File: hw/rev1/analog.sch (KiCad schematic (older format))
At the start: 69 parts, among them J1 80VAC, J2 CAP, J3 MOTOR, J5 TACHO, Q1 6N60C, Q2 2N5551, Q4 2N5551, U1 LM324, U2 LM311

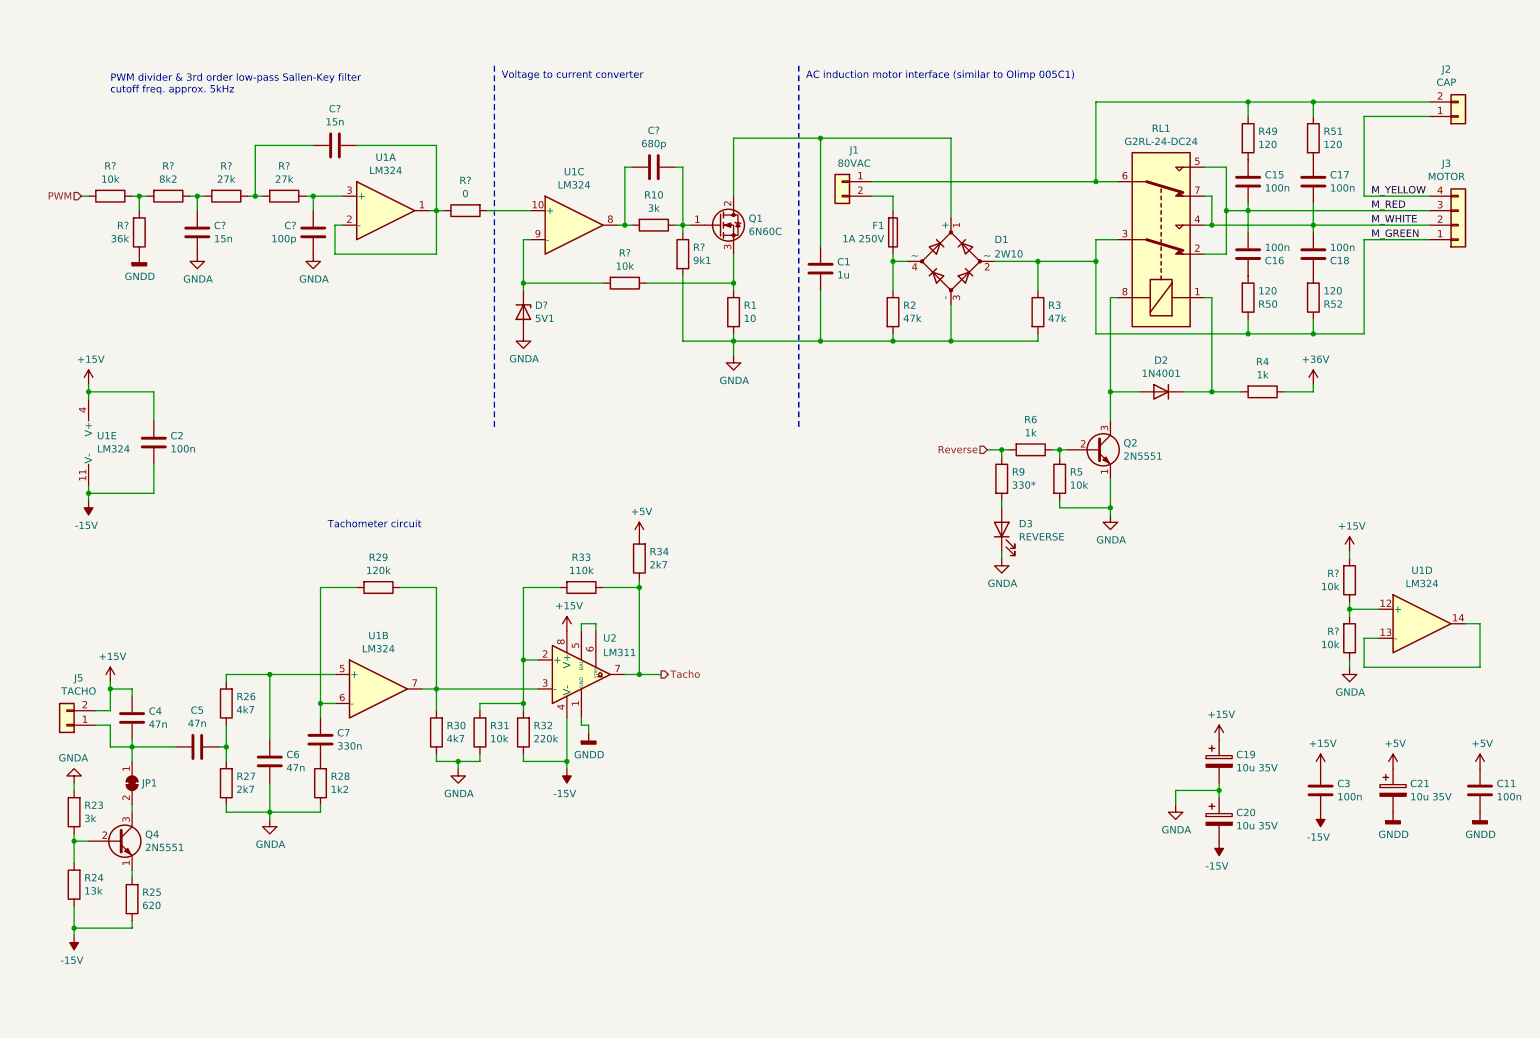
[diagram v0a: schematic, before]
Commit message: В схему добавлен забытый ZCD.
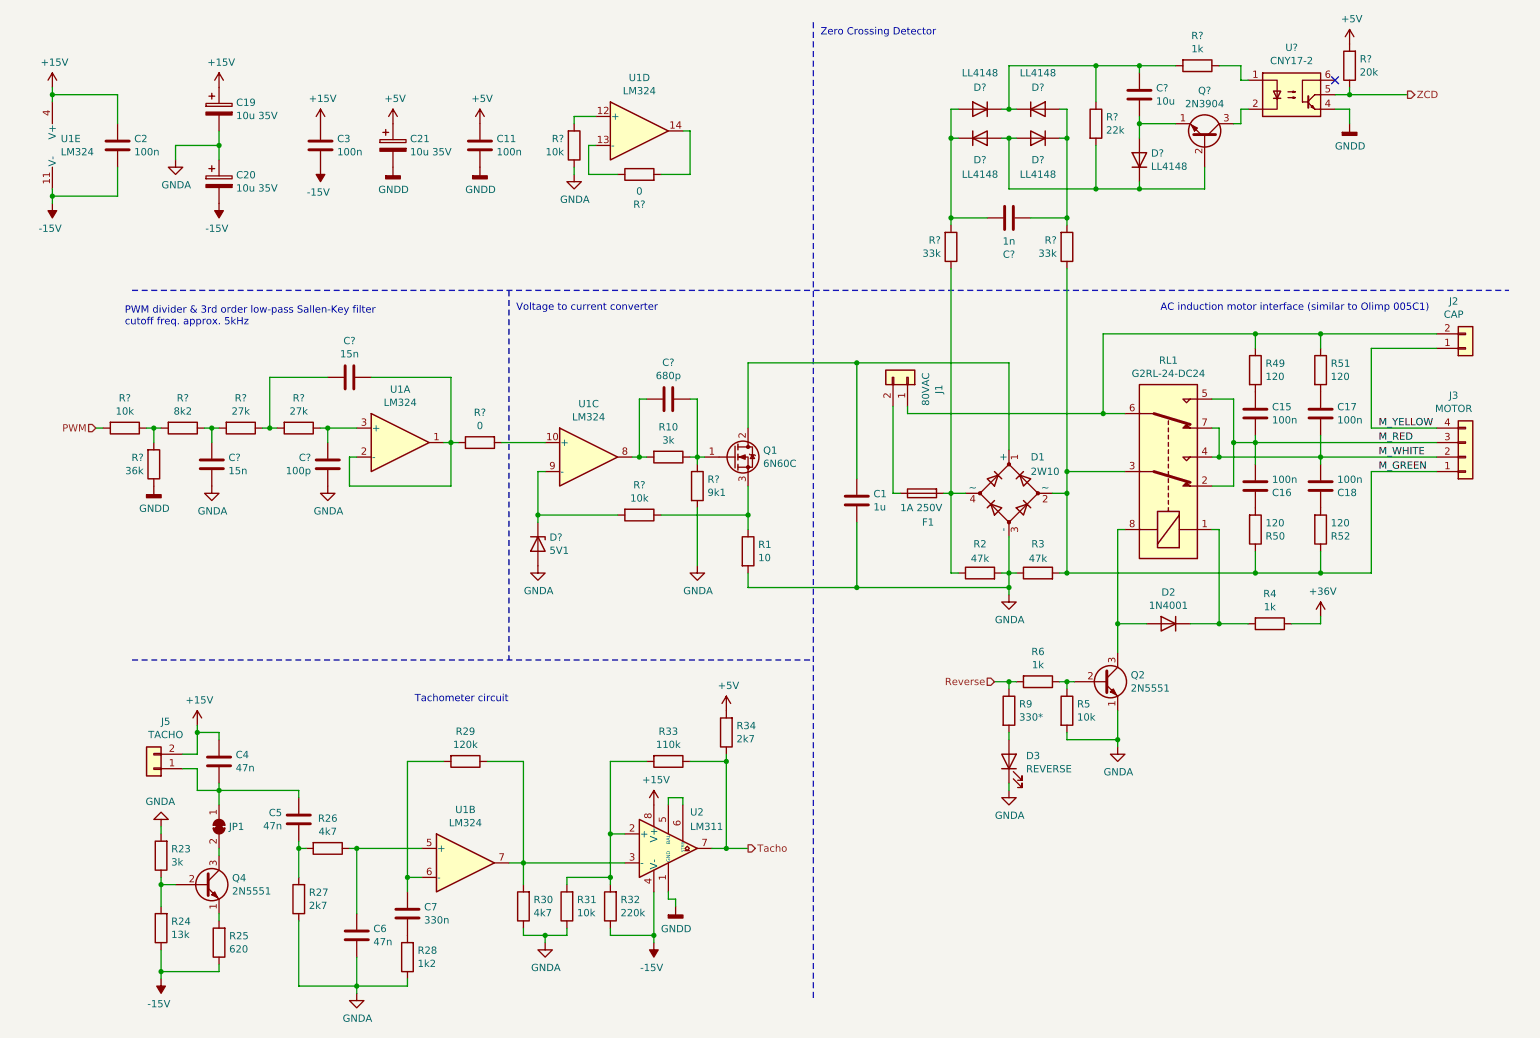
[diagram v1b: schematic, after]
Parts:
- removed R?: 10k, Resistor_SMD:R_0805_2012Metric, symbol Device:R
- added C?: 1n, Capacitor_SMD:C_0805_2012Metric, symbol Device:C
- added C?: 10u, Capacitor_SMD:C_0805_2012Metric, symbol Device:C
- added D? (x5): LL4148, Diode_SMD:D_MiniMELF, symbol Diode:LL4148
- added Q?: 2N3904, Package_TO_SOT_THT:TO-92_Inline, symbol Transistor_BJT:2N3904
- added R?: 0, Resistor_SMD:R_0805_2012Metric, symbol Device:R
- added R? (x2): 33k, Resistor_SMD:R_0805_2012Metric, symbol Device:R
- added R?: 22k, Resistor_THT:R_Axial_DIN0207_L6.3mm_D2.5mm_P10.16mm_Horizontal, symbol Device:R
- added R?: 1k, Resistor_THT:R_Axial_DIN0207_L6.3mm_D2.5mm_P10.16mm_Horizontal, symbol Device:R
- added R?: 20k, Resistor_SMD:R_0805_2012Metric, symbol Device:R
- added U?: CNY17-2, symbol Isolator:CNY17-2
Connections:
- net +15V: no longer R?.2
- net +5V: now also R?.2
- net GNDA: now also R3.1, R?.1; no longer R3.2
- net GNDD: now also U?.4
- net M_GREEN: now also R3.2, R?.1; no longer R3.1
- net at J1.2 (Pin_2): now also F1.1; no longer F1.2
- net at D1.4 (~~), R2.1: now also F1.2, R?.1; no longer F1.1
- net at C4.2, J5.1 (Pin_1), JP1.1 (A): now also C5.1; no longer C5.2
- net at C6.1, U1.5 (+): now also R26.1; no longer R26.2
- net at U1.12 (+): now also R?.2; no longer R?.1
- net at U1.13 (-): now also R?.1; no longer U1.14
- new net: R?.2, U1.14
- new net: C5.2, R26.2, R27.2
- new net: C?.2, D?.1 (K), D?.2 (A), R?.2
- new net: D?.1 (K), D?.2 (A), D?.2 (A), Q?.2 (B), R?.2
- new net: C?.1, D?.1 (K), D?.1 (K), R?.1, R?.2
- new net: C?.1, D?.1 (K), D?.2 (A), R?.2
- new net: C?.2, D?.2 (A), Q?.1 (E)
- new net: Q?.3 (C), U?.2
- new net: R?.1, U?.1
- new net ZCD: R?.1, U?.5
- no-connect marks 0 -> 1
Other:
- note added: "Zero Crossing Detector"
- moved on the sheet: C1, C11, C15, C16, C17, C18, C19, C2, C20, C21, C3, C4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

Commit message: Добавлена печатная плата rev1 (вероятно чистовая).
+ Обозначена и разведена схема ZCD;
+ Исключена схема аналогового перемножителя;
  * модуляция модулем синуса полностью цифровая;
+ LM324 использована полностью:
  * собран 2й PWM фильтр, подключенный к OC2A в отладочных целях;
+ Добавлен доп. светодиод, предназначенный для контроля за ZCD;
+ Исправлен разъем логических сигналов управления;
+ Всякие незначимые украшательства.
+ Немного документирована плата rev0.
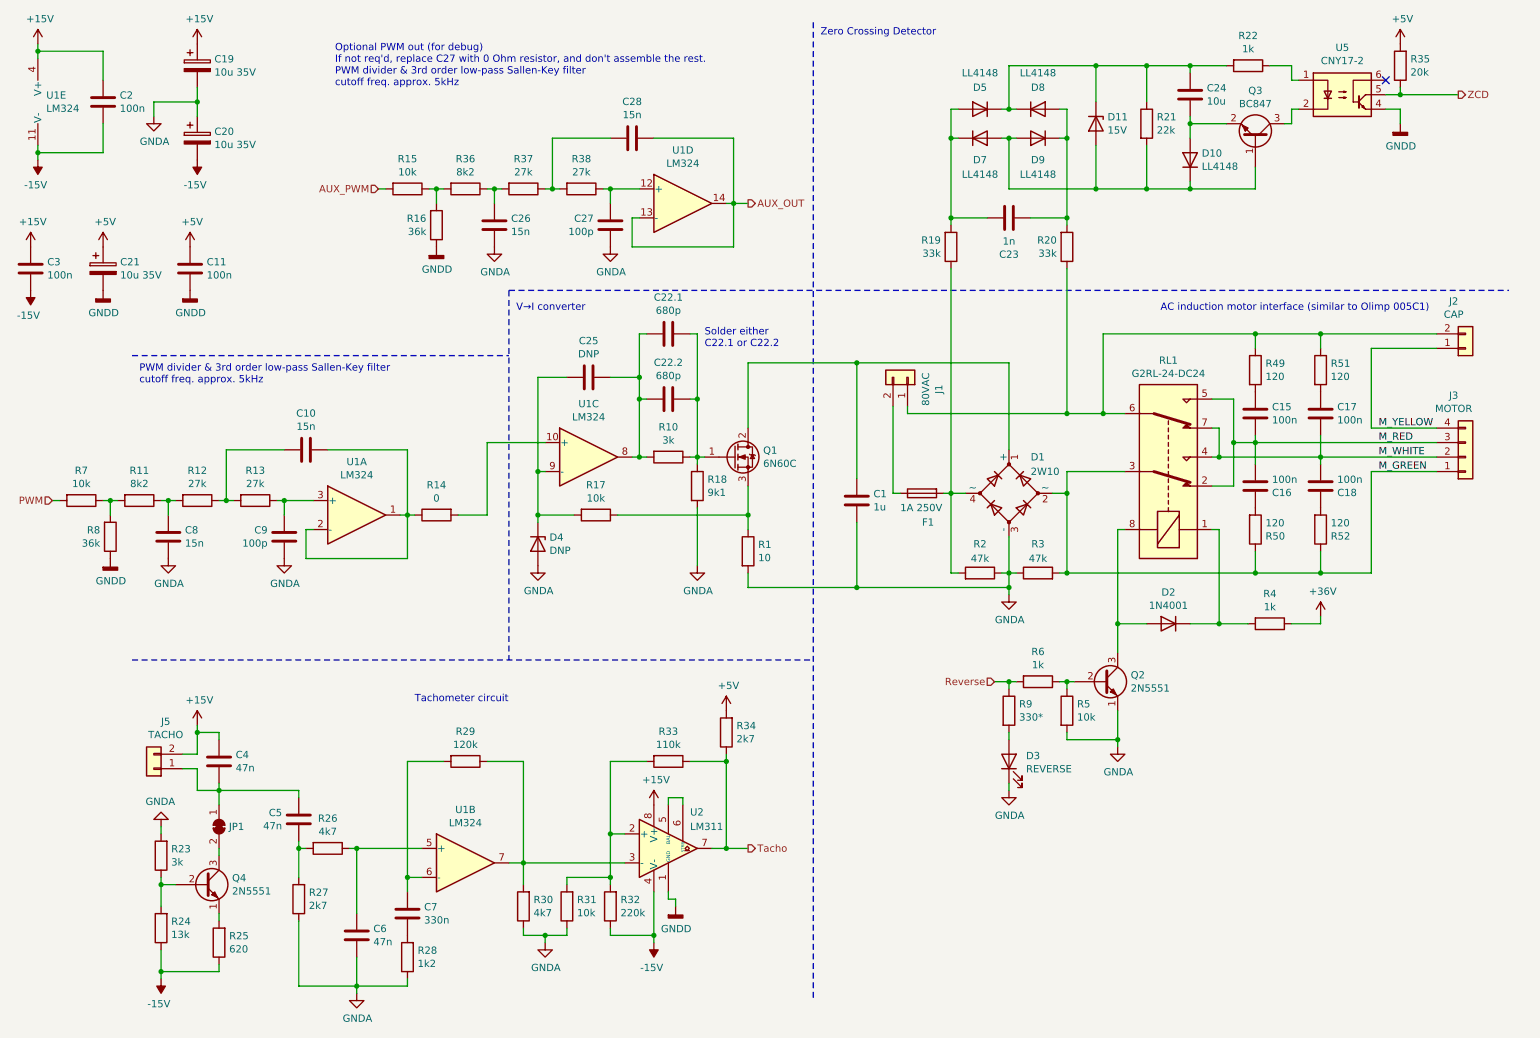
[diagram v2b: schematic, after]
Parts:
- removed Q?: 2N3904, Package_TO_SOT_THT:TO-92_Inline, symbol Transistor_BJT:2N3904
- removed R?: 0, Resistor_SMD:R_0805_2012Metric, symbol Device:R
- removed R?: 1k, Resistor_THT:R_Axial_DIN0207_L6.3mm_D2.5mm_P10.16mm_Horizontal, symbol Device:R
- removed R?: 10k, Resistor_SMD:R_0805_2012Metric, symbol Device:R
- added C22.1: 680p, Capacitor_THT:C_Rect_L7.0mm_W4.5mm_P5.00mm, symbol Device:C
- added C25: DNP, Capacitor_SMD:C_0805_2012Metric, symbol Device:C
- added C26, C28: 15n, Capacitor_SMD:C_0805_2012Metric, symbol Device:C
- added C27: 100p, Capacitor_SMD:C_0805_2012Metric, symbol Device:C
- added D11: 15V, Diode_SMD:D_SOD-123, symbol Device:D_Zener
- added Q3: BC847, Package_TO_SOT_SMD:SOT-23, symbol Transistor_BJT:BC847
- added R15: 10k, Resistor_SMD:R_0805_2012Metric, symbol Device:R
- added R16: 36k, Resistor_SMD:R_0805_2012Metric, symbol Device:R
- added R22: 1k, Resistor_SMD:R_1206_3216Metric, symbol Device:R
- added R36: 8k2, Resistor_SMD:R_0805_2012Metric, symbol Device:R
- added R37, R38: 27k, Resistor_SMD:R_0805_2012Metric, symbol Device:R
- C23, C24: renamed from C?; footprint Capacitor_SMD:C_0805_2012Metric -> Capacitor_SMD:C_1206_3216Metric
- D4: renamed from D?; value 5V1 -> DNP; footprint (none) -> Diode_SMD:D_SOD-123
- Q1: footprint to220:TO-220F-3_Horizontal_TabDown -> to220:TO-220F-3_Horizontal_TabDown_no_silk
- R19, R20: renamed from R?; footprint Resistor_SMD:R_0805_2012Metric -> Resistor_SMD:R_1206_3216Metric
- R21: renamed from R?; footprint Resistor_THT:R_Axial_DIN0207_L6.3mm_D2.5mm_P10.16mm_Horizontal -> Resistor_SMD:R_1206_3216Metric
- U5: renamed from U?; footprint (none) -> Package_DIP:DIP-6_W7.62mm_LongPads
- gave numbers to parts that had none: 18
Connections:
- net GNDA: now also R2.1, C26.2, C27.2; no longer R2.2
- net GNDD: now also R16.1
- net M_GREEN: no longer R20.1
- net at J1.1 (Pin_1), J2.2 (Pin_2), R49.1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: now also R20.1
- net at D1.4 (~~), F1.2, R19.1: now also R2.2; no longer R2.1
- net at C22.2.1, Q1.1 (G), R10.1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: now also C22.1.1
- net at C22.2.2, R10.2, U1.8: now also C22.1.2, C25.1
- net AUX_OUT: now reaches U1.13 (-)
- net AUX_OUT: now also U1.14, C28.1
- net at D4.1 (K), R17.2, U1.9 (-): now also C25.2
- net at D10.1 (K), D7.2 (A), D9.2 (A)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: now also D11.2 (A), Q3.1 (B)
- net at C24.1, D5.1 (K), D8.1 (K)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: now also D11.1 (K), R22.2
- net at C24.2, D10.2 (A): now also Q3.2 (E)
- net at U5.2: now also Q3.3 (C)
- net at U5.1: now also R22.1
- net at U1.12 (+): now also C27.1, R38.1
- new net: C28.2, R37.1, R38.2
- new net: C26.1, R36.1, R37.2
- new net: R15.1, R16.2, R36.2
- new net AUX_PWM: R15.2
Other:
- note added: "Optional PWM out (for debug)\nIf not req'd, replace C27 with 0 Ohm resistor, and don't assemble the rest.\nPWM divider & 3rd order low-pass Sallen-Key filter\ncutoff freq. approx. 5kHz"
- note added: "Solder either\nC22.1 or C22.2"
- note added: "V→I converter"
- note removed: "Voltage to current converter"
- moved on the sheet: C10, C11, C19, C2, C20, C21, C24, C3, C8, C9, D10, R11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
